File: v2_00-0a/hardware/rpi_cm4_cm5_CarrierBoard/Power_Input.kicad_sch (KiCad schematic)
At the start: 0 parts

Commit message: Add design notes (power table) and latest changes to power supply and power input
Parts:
- added C114, C117, C119, C120, C121: 22u, footprint:CAP_NONPOL_0805, symbol KicadCompDb:Capacitors/CAP_CER_SMT_00011
- added C122: 0.1u, footprint:CAP_NONPOL_0402, symbol KicadCompDb:Capacitors/CAP_CER_SMT_00001
- added D11, D18, D20: SK34A-LTP, footprint:DO-214AC, symbol KicadCompDb:Diodes/DIODE_00005
- added D17: MMSZ5242B-TP, footprint:SOD-123, symbol KicadCompDb:Diodes/DIODE_00003
- added D19: SML4761A-E3/5A, footprint:DO-214AC, symbol KicadCompDb:Diodes/DIODE_00008
- added Q9: IPD60R360P7ATMA1, footprint:TO-252-3, symbol KicadCompDb:Mosfet/MOSFET_00005
- added R179, R180: 1K, footprint:RES_0402, symbol KicadCompDb:Resistors/RES_SMT_00004
- added R181: 470R, footprint:RES_0402, symbol KicadCompDb:Resistors/RES_SMT_00019
- added R182: 22R, footprint:RES_0402, symbol KicadCompDb:Resistors/RES_SMT_00015
- added R183, R184: 0R, footprint:RES_1206, symbol KicadCompDb:Resistors/RES_SMT_00022
- added U23: LTC4359IDCB, footprint:6-WFDFN-EP, symbol KicadCompDb:Miscellaneous/MISC_00006
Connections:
- new net: C122.2, D19.1 (K), R179.1, U23.1 (OUT)
- new net: C122.1, D18.2 (A), D19.2 (A), D20.2 (A), U23.6 (VSS), U23.7 (PAD)
- new net: C114.2, C117.2, C119.2, C120.2, C121.2, R183.2, R184.2
- new net: D11.2 (A), D17.2 (A), D20.1 (K), Q9.3 (S), R180.2, R181.2, U23. (SRC)
- new net: D17.1 (K), R182.1, U23.2 (GATE)
- new net: R181.1, U23.4 (IN)
- new net: R180.1, U23.5 (~{SHDN})
- new net: D11.1 (K), Q9.2 (D), R179.2, R183.1, R184.1
- new net: Q9.1 (G), R182.2
- new net CGND: D18.1 (K)
- new net GND: C114.1, C117.1, C119.1, C120.1, C121.1
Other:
- note added: "Depopulate 0R for I(meas)"

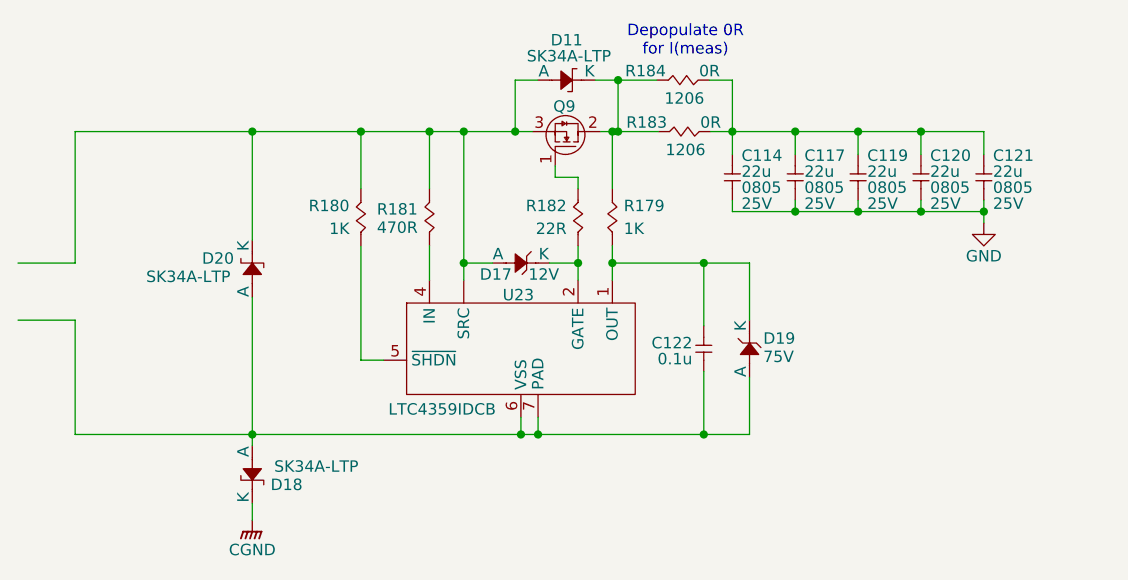
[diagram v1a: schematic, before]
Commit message: Add TFT schematic pages (power + connector)
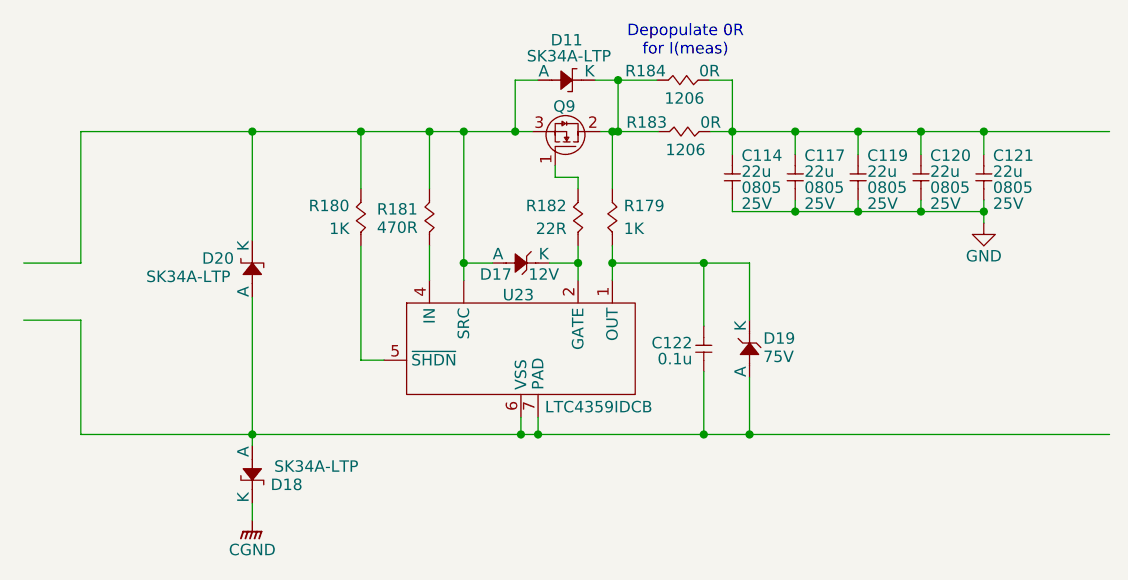
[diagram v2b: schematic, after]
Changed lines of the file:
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@@
+	)
+	(junction
+		(at 189.23 75.565)
+		(diameter 0)
+		(color 0 0 0 0)
 	)
 	(junction
@@
 	)
 	(junction
+		(at 163.195 109.22)
+		(diameter 0)
+		(color 0 0 0 0)
+	)
+	(junction
 		(at 137.16 75.565)
 		(diameter 0)
@@
 	(wire
 		(pts
+			(xy 107.95 109.22) (xy 137.795 109.22)
+		)
+		(stroke
+			(width 0)
+			(type default)
+		)
+	)
+	(wire
+		(pts
 			(xy 147.955 75.565) (xy 148.59 75.565)
 		)
@@
 	(wire
 		(pts
-			(xy 88.265 96.52) (xy 88.265 109.22)
+			(xy 88.9 96.52) (xy 88.9 109.22)
 		)
 		(stroke
@@
 	(wire
 		(pts
-			(xy 81.915 96.52) (xy 88.265 96.52)
+			(xy 82.55 96.52) (xy 88.9 96.52)
 		)
 		(stroke
@@
 	(wire
 		(pts
+			(xy 189.23 75.565) (xy 203.2 75.565)
+		)
+		(stroke
+			(width 0)
+			(type default)
+		)
+	)
+	(wire
+		(pts
 			(xy 140.97 90.17) (xy 144.145 90.17)
 		)
@@
 	(wire
 		(pts
-			(xy 88.265 109.22) (xy 107.95 109.22)
+			(xy 107.95 75.565) (xy 120.015 75.565)
+		)
+		(stroke
+			(width 0)
+			(type default)
+		)
+	)
+	(wire
+		(pts
+			(xy 88.9 109.22) (xy 107.95 109.22)
 		)
 		(stroke
@@
 	(wire
 		(pts
+			(xy 163.195 109.22) (xy 203.2 109.22)
+		)
+		(stroke
+			(width 0)
+			(type default)
+		)
+	)
+	(wire
+		(pts
 			(xy 141.605 79.375) (xy 141.605 80.645)
 		)
@@
 	(wire
 		(pts
-			(xy 107.95 109.22) (xy 137.795 109.22)
-		)
-		(stroke
-			(width 0)
-			(type default)
-		)
-	)
-	(wire
-		(pts
 			(xy 127.635 88.265) (xy 127.635 92.075)
 		)
@@
 	(wire
 		(pts
-			(xy 107.95 75.565) (xy 120.015 75.565)
-		)
-		(stroke
-			(width 0)
-			(type default)
-		)
-	)
-	(wire
-		(pts
 			(xy 168.275 75.565) (xy 175.26 75.565)
 		)
@@
 	(wire
 		(pts
-			(xy 81.915 90.17) (xy 88.265 90.17)
+			(xy 82.55 90.17) (xy 88.9 90.17)
 		)
 		(stroke
@@
 	(wire
 		(pts
-			(xy 88.265 75.565) (xy 107.95 75.565)
+			(xy 88.9 75.565) (xy 107.95 75.565)
 		)
 		(stroke
@@
 	(wire
 		(pts
-			(xy 88.265 75.565) (xy 88.265 90.17)
+			(xy 88.9 75.565) (xy 88.9 90.17)
 		)
 		(stroke
@@
 		)
 		(property "Value" "LTC4359IDCB"
-			(at 123.063 106.426 0)
-			(effects
-				(font
+			(at 140.462 106.172 0)
+			(effects
+				(font

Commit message: Update schematic
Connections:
- net at C114.2, C117.2, C119.2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: no longer R183.2, R184.2

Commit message: Add and modify existing schematics
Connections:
- net at C114.2, C117.2, C119.2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: now also R183.2, R184.2
- net at D11.2 (A), D17.2 (A), D20.1 (K)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: now also U23.3 (SRC); no longer U23. (SRC)
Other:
- note added: "Resistors are 1% 1/16W 0402 unless otherwise noted Capacitors are 10% 50V X7R 0402 unless otherwise noted"
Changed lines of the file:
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@@
 		(comment 8 "WIP")
 	)
+	(text "Resistors are 1% 1/16W 0402 unless otherwise noted\nCapacitors are 10% 50V X7R 0402 unless otherwise noted"
+		(exclude_from_sim no)
+		(at 12.7 170.942 0)
+		(effects
+			(font
+				(size 1.27 1.27)
+			)
+			(justify left)
+		)
+	)
 	(text "Depopulate 0R\nfor I(meas)"
 		(exclude_from_sim no)
@@
 	(wire
 		(pts
+			(xy 159.385 69.85) (xy 161.29 69.85)
+		)
+		(stroke
+			(width 0)
+			(type default)
+		)
+	)
+	(wire
+		(pts
 			(xy 120.015 75.565) (xy 127.635 75.565)
 		)
@@
 	(wire
 		(pts
-			(xy 161.29 75.565) (xy 168.275 75.565)
+			(xy 159.385 75.565) (xy 161.29 75.565)
 		)
 		(stroke
@@
 	(wire
 		(pts
-			(xy 88.9 75.565) (xy 107.95 75.565)
+			(xy 161.29 75.565) (xy 168.275 75.565)
 		)
 		(stroke
@@
 	(wire
 		(pts
-			(xy 158.877 75.565) (xy 161.29 75.565)
+			(xy 88.9 75.565) (xy 107.95 75.565)
 		)
 		(stroke
@@
 	(wire
 		(pts
-			(xy 141.605 80.645) (xy 144.145 80.645)
+			(xy 148.59 69.85) (xy 153.035 69.85)
 		)
 		(stroke
@@
 	(wire
 		(pts
-			(xy 147.955 75.565) (xy 147.955 81.915)
+			(xy 141.605 80.645) (xy 144.145 80.645)
 		)
 		(stroke
@@
 	(wire
 		(pts
-			(xy 158.75 69.85) (xy 161.29 69.85)
+			(xy 147.955 75.565) (xy 147.955 81.915)
 		)
 		(stroke
@@
 		)
 	)
-	(wire
-		(pts
-			(xy 148.59 69.85) (xy 152.908 69.85)
+	(netclass_flag ""
+		(length 2.54)
+		(shape diamond)
+		(at 189.23 75.565 0)
+		(fields_autoplaced yes)
+		(effects
+			(font
+				(size 1.27 1.27)
+				(color 255 0 0 1)
+			)
+			(justify left bottom)
 		)
-		(stroke
-			(width 0)
-			(type default)
+		(property "Netclass" "POWER_PLANE"
+			(at 190.4365 73.025 0)
+			(effects
+				(font
+					(size 1.27 1.27)
+					(color 255 0 0 1)
+				)
+				(justify left)
+			)
+		)
+		(property "Component Class" ""
+			(at -37.465 45.085 0)
+			(effects
+				(font
+					(size 1.27 1.27)
+					(italic yes)
+				)
+			)
+		)
+	)
+	(netclass_flag ""
+		(length 2.54)
+		(shape diamond)
+		(at 107.95 75.565 0)
+		(fields_autoplaced yes)
+		(effects
+			(font
+				(size 1.27 1.27)
+				(color 255 0 0 1)
+			)
+			(justify left bottom)
+		)
+		(property "Netclass" "POWER_PLANE"
+			(at 109.1565 73.025 0)
+			(effects
+				(font
+					(size 1.27 1.27)
+					(color 255 0 0 1)
+				)
+				(justify left)
+			)
+		)
+		(property "Component Class" ""
+			(at -118.745 45.085 0)
+			(effects
+				(font
+					(size 1.27 1.27)
+					(italic yes)
+				)
+			)
 		)
 	)
@@
 		(pin "1"
 		)
-		(pin ""
+		(pin "3"
 		)
 		(pin "7"
@@
 	(symbol
 		(lib_id "KicadCompDb:Resistors/RES_SMT_00022")
-		(at 154.178 69.85 0)
+		(at 154.305 69.85 0)
 		(unit 1)
 		(exclude_from_sim no)
@@
 		(dnp no)
 		(property "Reference" "R184"
-			(at 151.638 68.834 0)
+			(at 151.765 68.834 0)
 			(effects
 				(font
@@
 		)
 		(property "Value" "0R"
-			(at 158.75 68.834 0)
+			(at 158.877 68.834 0)
 			(effects
 				(font
@@
 		)
 		(property "Footprint" "footprint:RES_1206"
-			(at 154.686 91.948 0)
+			(at 154.813 91.948 0)
 			(effects
 				(font
@@
 		)
 		(property "Datasheet" "https://www.yageogroup.com/content/datasheet/asset/file/PYU-RC_GROUP_51_ROHS_L"
-			(at 154.178 69.85 0)
+			(at 154.305 69.85 0)
 			(effects
 				(font
@@
 		)
 		(property "Description" "RES 0 OHM JUMPER 1/4W 1206"
-			(at 155.956 79.756 0)
+			(at 156.083 79.756 0)
 			(effects
 				(font
@@
 		)
 		(property "Tolerance" "1%"
-			(at 155.829 64.135 0)
+			(at 155.956 64.135 0)
 			(effects
 				(font
@@
 		)
 		(property "Power" "1/4W"
-			(at 155.829 66.675 0)
+			(at 155.956 66.675 0)
 			(effects
 				(font
@@
 		)
 		(property "Package" "1206"
-			(at 155.956 71.882 0)
+			(at 156.083 71.882 0)
 			(effects
 				(font
@@
 		)
 		(property "Manufacturer" "YAGEO"
-			(at 154.432 88.138 0)
+			(at 154.559 88.138 0)
 			(effects
 				(font
@@
 		)
 		(property "Manufacturer Part Number" "RC1206JR-070RL"
-			(at 154.432 77.724 0)
+			(at 154.559 77.724 0)
 			(effects
 				(font
@@
 		)
 		(property "Distributor" "DigiKey"
-			(at 154.178 75.692 0)
+			(at 154.305 75.692 0)
 			(effects
 				(font
@@
 		)
 		(property "Distributor Part Number" "311-0.0ERCT-ND"
-			(at 154.94 82.042 0)
+			(at 155.067 82.042 0)
 			(effects
 				(font
@@
 		)
 		(property "Temperature Coefficient" "±100ppm/°C"
-			(at 154.178 69.85 0)
+			(at 154.305 69.85 0)
 			(effects
 				(font
@@
 		)
 		(property "Operating Temperature" "-55°C ~ 155°C"
-			(at 154.94 94.234 0)
+			(at 155.067 94.234 0)
 			(effects
 				(font
@@
 		)
 		(property "Type" "RES SMT"
-			(at 154.178 69.85 0)
+			(at 154.305 69.85 0)
 			(show_name yes)
 			(effects
@@
 		)
 		(property "Dimensions" "3.10mm x 1.60mm"
-			(at 154.178 69.85 0)
+			(at 154.305 69.85 0)
 			(show_name yes)
 			(effects
